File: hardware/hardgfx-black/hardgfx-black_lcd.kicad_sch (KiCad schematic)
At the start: 28 parts, among them J12 FH12-50S-0.5SH, J13 FH12-10S-0.5SH, J14 ~{LCD_RST}, J15 ~{LCD_WAKE}, J16 MODE, J17 LR, J18 UD, J19 DITH, U8 TPS61041DBV

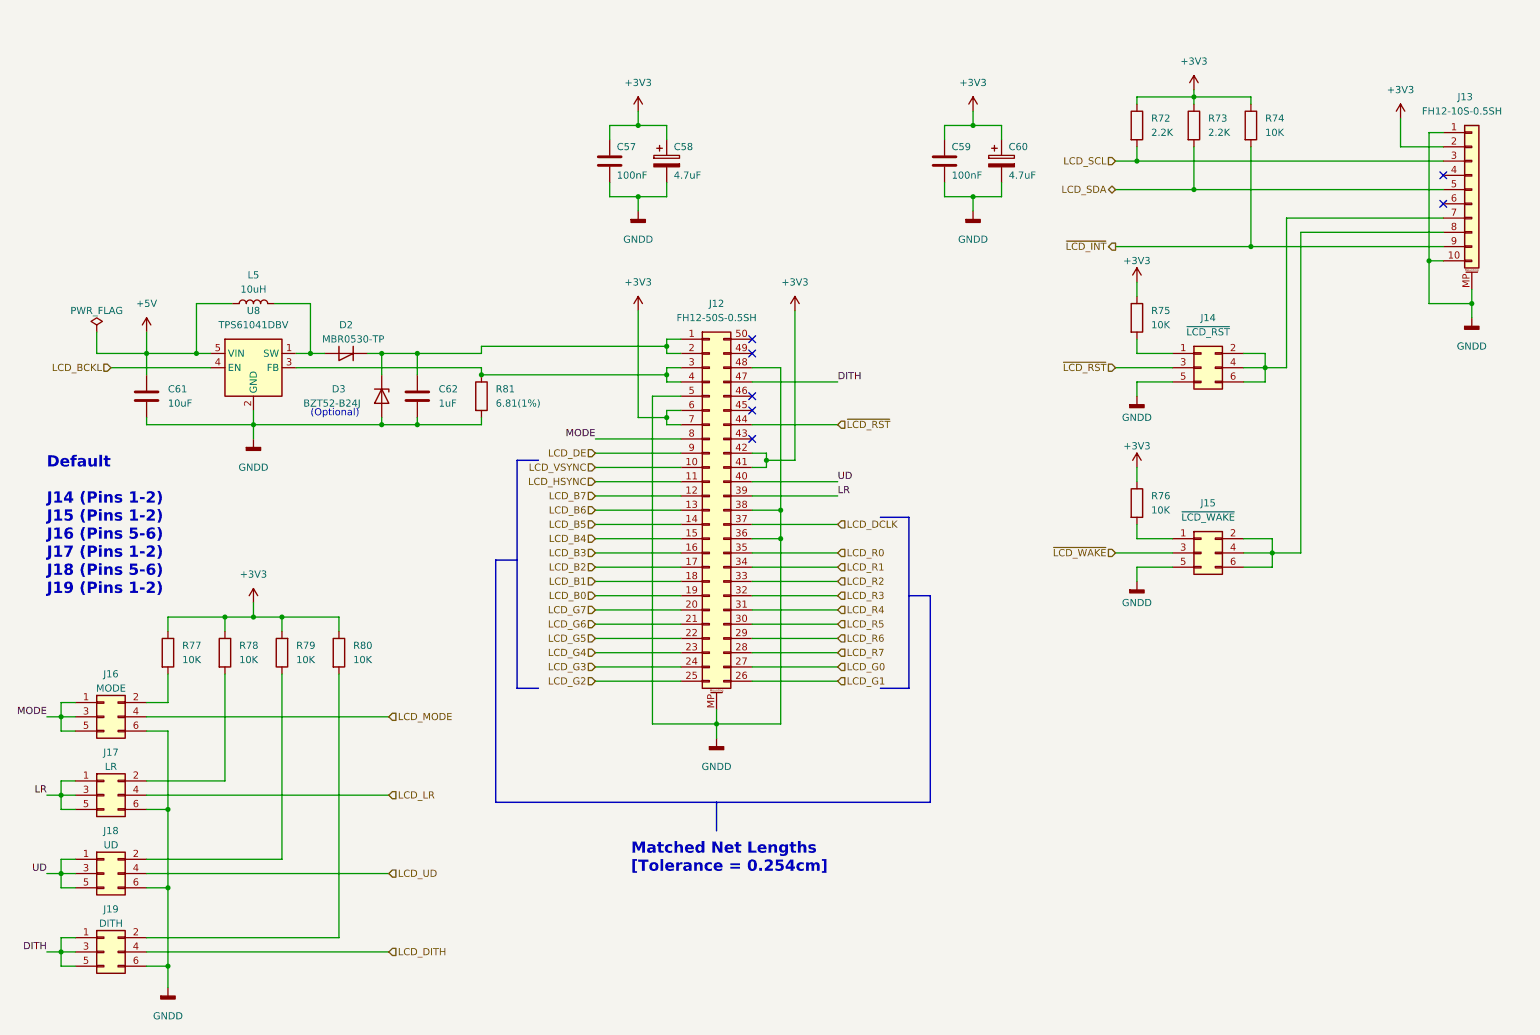
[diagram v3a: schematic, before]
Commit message: Added generic SDRAM configuration using macros.
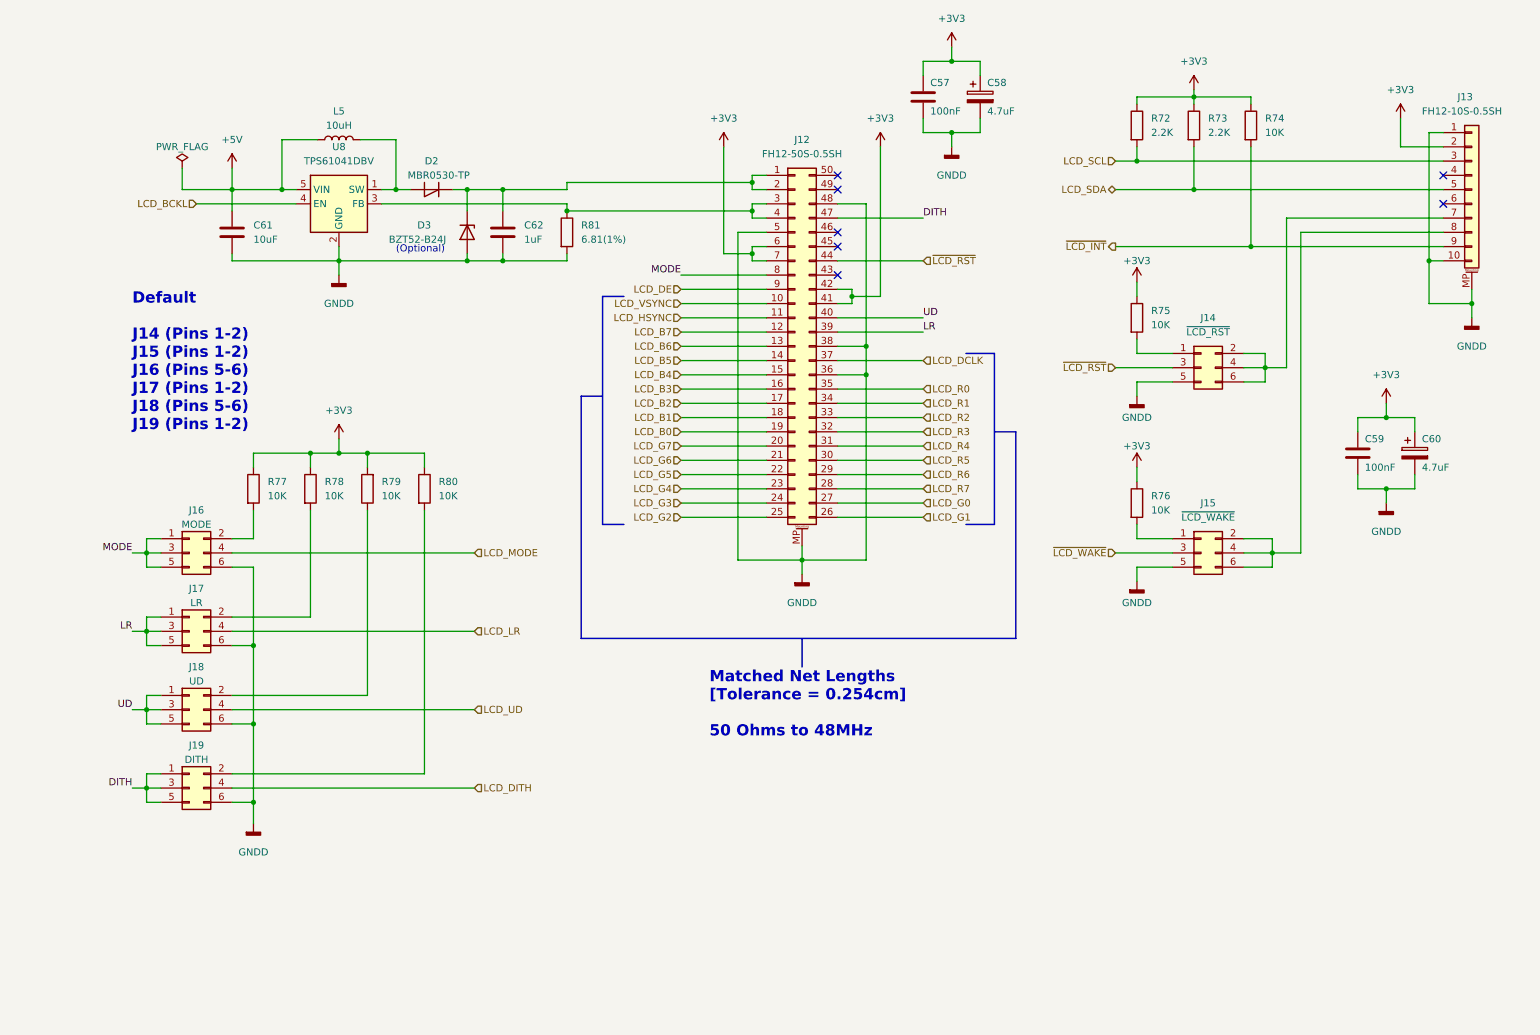
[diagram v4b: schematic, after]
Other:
- note added: "Matched Net Lengths [Tolerance = 0.254cm] 50 Ohms to 48MHz"
- note removed: "Matched Net Lengths [Tolerance = 0.254cm]"
- moved on the sheet: C57, C58, C59, C60, C61, C62, D2, D3, J12, J16, J17, J18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
